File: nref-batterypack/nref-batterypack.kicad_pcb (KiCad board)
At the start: 2 copper layers, 75 x 18 mm, 6 parts

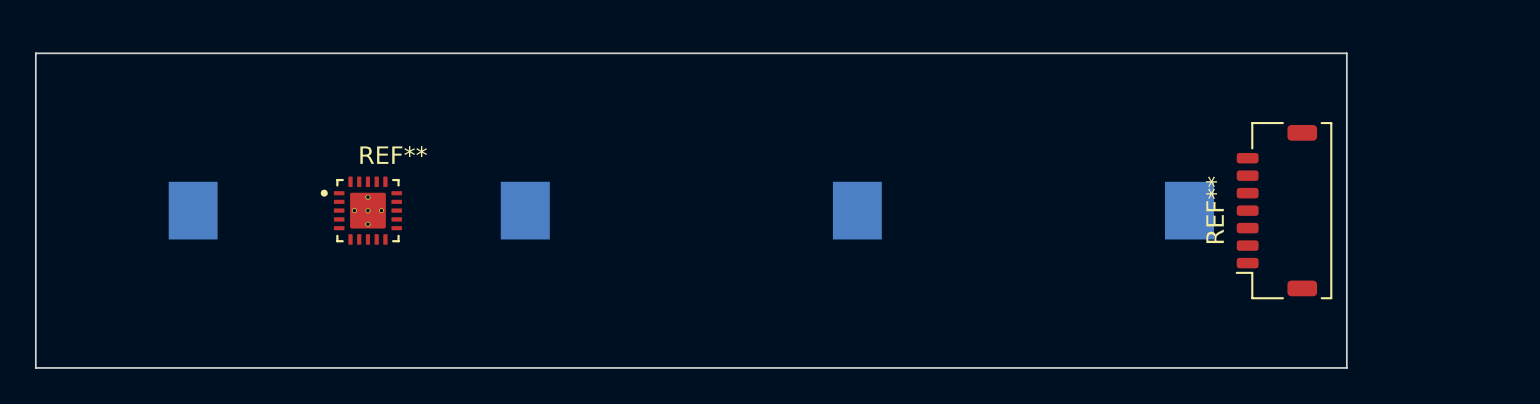
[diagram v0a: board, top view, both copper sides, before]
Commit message: add initial 4S battery pack with hs-switch
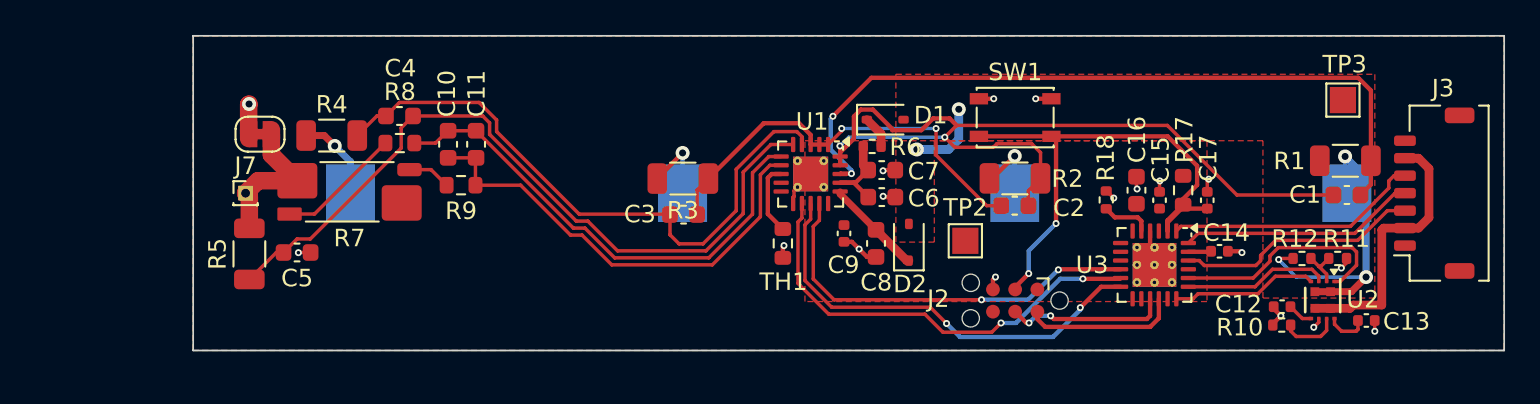
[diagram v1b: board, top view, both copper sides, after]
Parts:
- removed J** (x4): S713145R, footprints:S713145R
- removed REF**: JST_SHL_SM07B-SHLS-TF_1x07-1MP_P1.00mm_Horizontal, Connector_JST:JST_SHL_SM07B-SHLS-TF_1x07-1MP_P1.00mm_Horizontal
- removed REF**: IC_BQ76905RGRR, footprints:IC_BQ76905RGRR
- added C1: 220nF, Capacitor_SMD:C_0603_1608Metric, F.Cu at (166.0, 99.1)
- added C10: 100pF, Capacitor_SMD:C_0603_1608Metric, F.Cu at (114.6, 96.2)
- added C11: 100nF, Capacitor_SMD:C_0603_1608Metric, F.Cu at (116.2, 96.2)
- added C12: 2.2nF, Capacitor_SMD:C_0402_1005Metric, F.Cu at (162.3, 105.5)
- added C13: DNP, Capacitor_SMD:C_0402_1005Metric, F.Cu at (167.1, 106.3)
- added C14: 0.47uF, Capacitor_SMD:C_0402_1005Metric, F.Cu at (158.7, 102.3)
- added C15: 100nF, Capacitor_SMD:C_0402_1005Metric, F.Cu at (155.3, 99.4)
- added C16: 10uF, Capacitor_SMD:C_0603_1608Metric, F.Cu at (154.0, 98.8)
- added C17: 100nF, Capacitor_SMD:C_0402_1005Metric, F.Cu at (158.0, 99.4)
- added C2: 220nF, Capacitor_SMD:C_0603_1608Metric, F.Cu at (147.0, 99.7)
- added C3: 220nF, Capacitor_SMD:C_0603_1608Metric, F.Cu at (128.1, 100.2)
- added C4: 220nF, Capacitor_SMD:C_0603_1608Metric, F.Cu at (111.8, 94.6)
- added C5: 220nF, Capacitor_SMD:C_0603_1608Metric, F.Cu at (105.9, 102.4)
- added C6: 100pF/25V, Capacitor_SMD:C_0603_1608Metric, F.Cu at (139.4, 99.2)
- added C7: 1uF/25V, Capacitor_SMD:C_0603_1608Metric, F.Cu at (139.4, 97.7)
- added C8: 1uF/25V, Capacitor_SMD:C_0603_1608Metric, F.Cu at (139.1, 101.9)
- added C9: 1uF, Capacitor_SMD:C_0402_1005Metric, F.Cu at (137.2, 101.3)
- added D1: 40V, Diode_SMD:D_SOD-323, F.Cu at (139.6, 94.8)
- added D2: 40V, Diode_SMD:D_SOD-323, F.Cu at (140.9, 101.8)
- added J1: C3+, footprints:S713145R, B.Cu at (147.0, 99.0)
- added J2: DBG, Connector:Tag-Connect_TC2030-IDC-NL_2x03_P1.27mm_Vertical, F.Cu at (147.0, 105.1)
- added J3: PACK_CONN, Connector_JST:JST_SHL_SM07B-SHLS-TF_1x07-1MP_P1.00mm_Horizontal, F.Cu at (171.0, 99.0)
- added J4: C4+, footprints:S713145R, B.Cu at (166.0, 99.0)
- added J5: C2+, footprints:S713145R, B.Cu at (128.0, 99.0)
- added J6: C1+, footprints:S713145R, B.Cu at (109.0, 99.0)
- added J7: C1-, Connector_PinHeader_1.00mm:PinHeader_1x01_P1.00mm_Vertical, F.Cu at (103.0, 99.0)
- added NT1: P- to GND, Jumper:SolderJumper-2_P1.3mm_Bridged_RoundedPad1.0x1.5mm, F.Cu at (103.8, 95.6)
- added R1: 10R, Resistor_SMD:R_1206_3216Metric, F.Cu at (165.9, 97.1)
- added R10: 866R, Resistor_SMD:R_0402_1005Metric, F.Cu at (162.3, 106.5)
- added R11: 14.7k, Resistor_SMD:R_0402_1005Metric, F.Cu at (165.5, 102.7)
- added R12: 470k, Resistor_SMD:R_0402_1005Metric, F.Cu at (163.4, 102.7)
- added R17: 100R, Resistor_SMD:R_0603_1608Metric, F.Cu at (156.6, 98.8)
- added R18: 100k/0.1%/25ppm, Resistor_SMD:R_0402_1005Metric, F.Cu at (152.2, 99.4)
- added R2: 10R, Resistor_SMD:R_1206_3216Metric, F.Cu at (147.0, 98.2)
- added R3: 10R, Resistor_SMD:R_1206_3216Metric, F.Cu at (128.0, 98.2)
- added R4: 10R, Resistor_SMD:R_1206_3216Metric, F.Cu at (107.9, 95.7)
- added R5: 10R, Resistor_SMD:R_1206_3216Metric, F.Cu at (103.2, 102.5)
- added R6: 100R, Resistor_SMD:R_0402_1005Metric, F.Cu at (138.8, 96.3)
- added R7: 1u, Resistor_SMD:R_Shunt_Vishay_WSK2512_6332Metric_T1.19mm, F.Cu at (108.9, 98.9)
- added R8: 100R, Resistor_SMD:R_0603_1608Metric, F.Cu at (111.8, 96.1)
- added R9: 100R, Resistor_SMD:R_0603_1608Metric, F.Cu at (115.3, 98.5)
- added SW1: Reset, Button_Switch_SMD:SW_SPST_PTS810, F.Cu at (147.0, 94.7)
- added TH1: Thermistor, Resistor_SMD:R_0603_1608Metric, F.Cu at (133.7, 101.9)
- added TP2: 3V3, TestPoint:TestPoint_Pad_1.5x1.5mm, F.Cu at (144.2, 101.7)
- added TP3: Pack Voltage, TestPoint:TestPoint_Pad_1.5x1.5mm, F.Cu at (165.8, 93.7)
- added U1: BQ76905, Package_DFN_QFN:QFN-20-1EP_3.5x3.5mm_P0.5mm_EP2x2mm_ThermalVias, F.Cu at (135.3, 97.9)
- added U2: TPS259482, Automated:PowerWCSP12_YWP_TEX, F.Cu at (164.6, 105.1)
- added U3: MSPM0L130xRGE, Package_DFN_QFN:VQFN-24-1EP_4x4mm_P0.5mm_EP2.5x2.5mm_ThermalVias, F.Cu at (155.0, 103.1)
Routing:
- net Net-(U1-VC4A): track 0.00 -> 50.9 mm, vias 0 -> 2
- net Net-(U1-VC0): track 0.00 -> 43.1 mm
- net Net-(U1-VC5): track 0.00 -> 42.7 mm, vias 0 -> 2
- net Net-(U1-VC1): track 0.00 -> 35.3 mm
- net /~{RST}: track 0.00 -> 30.5 mm, vias 0 -> 2
- net Net-(U1-SRP): track 0.00 -> 28.1 mm
- net Net-(U1-SRN): track 0.00 -> 26.3 mm
- net /SCL_{DEV}: track 0.00 -> 25.6 mm, vias 0 -> 2
- net /SDA_{DEV}: track 0.00 -> 25.2 mm, vias 0 -> 2
- net Net-(U1-VC2): track 0.00 -> 24.4 mm, vias 0 -> 2
- net IN: track 0.00 -> 23.4 mm, vias 0 -> 5
- net /ALERT: track 0.00 -> 23.3 mm, vias 0 -> 2
- net GND: track 0.00 -> 20.3 mm, vias 0 -> 18
- net /V_{OUT}: track 0.00 -> 15.6 mm
- net /SCL_{HOST}: track 0.00 -> 14.6 mm
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- added copper zone on F.Cu, net +3V3
- added copper zone on F.Cu, net /PACK-
- added copper zone on B.Cu, net GND
- added copper zone on F.Cu, net IN
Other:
- board text removed: "consider S7091-42R (gold plated)"

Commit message: wip of the new version with another bms ic
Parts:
- removed C12: 2.2nF, Capacitor_SMD:C_0402_1005Metric
- removed C2, C3, C4, C5: 220nF, Capacitor_SMD:C_0603_1608Metric
- removed C8: 1uF/25V, Capacitor_SMD:C_0603_1608Metric
- removed J2: DBG, Connector:Tag-Connect_TC2030-IDC-NL_2x03_P1.27mm_Vertical
- removed TP2: 3V3, TestPoint:TestPoint_Pad_1.5x1.5mm
- removed U1: BQ76905, Package_DFN_QFN:QFN-20-1EP_3.5x3.5mm_P0.5mm_EP2x2mm_ThermalVias
- removed U2: TPS259482, Automated:PowerWCSP12_YWP_TEX
- removed U3: MSPM0L130xRGE, Package_DFN_QFN:VQFN-24-1EP_4x4mm_P0.5mm_EP2.5x2.5mm_ThermalVias
- added D3: 30V, Diode_SMD:D_SOD-323F, F.Cu at (157.8, 97.2)
- added D4: 30V, Diode_SMD:D_SOD-323F, F.Cu at (143.3, 97.5)
- added D5: 30V, Diode_SMD:D_SOD-323F, F.Cu at (123.7, 103.6)
- added D6: 30V, Diode_SMD:D_SOD-323F, F.Cu at (109.6, 105.0)
- added Q1: BC817, Package_TO_SOT_SMD:SOT-23, F.Cu at (157.7, 94.3)
- added Q10: 30V, Package_SON:Diodes_PowerDI3333-8, F.Cu at (130.9, 82.9)
- added Q2: BC817, Package_TO_SOT_SMD:SOT-23, F.Cu at (142.6, 94.7)
- added Q3: BC817, Package_TO_SOT_SMD:SOT-23, F.Cu at (123.7, 100.7)
- added Q4: BC817, Package_TO_SOT_SMD:SOT-23, F.Cu at (106.5, 102.7)
- added Q5: AO3401A, Package_TO_SOT_SMD:SOT-23, F.Cu at (135.9, 77.9)
- added Q6: AO3401A, Package_TO_SOT_SMD:SOT-23, F.Cu at (135.9, 82.5)
- added Q9: 30V, Package_SON:Diodes_PowerDI3333-8, F.Cu at (130.9, 78.0)
- added R13: 49.9R, Resistor_SMD:R_1206_3216Metric, F.Cu at (147.0, 95.2)
- added R14: 240R, Resistor_SMD:R_0603_1608Metric, F.Cu at (144.2, 100.0)
- added R15: 100R, Resistor_SMD:R_0603_1608Metric, F.Cu at (142.6, 100.0)
- added R16: 49.9R, Resistor_SMD:R_1206_3216Metric, F.Cu at (128.0, 100.1)
- added R19: 100R, Resistor_SMD:R_0603_1608Metric, F.Cu at (127.2, 103.6)
- added R20: 49.9R, Resistor_SMD:R_1206_3216Metric, F.Cu at (111.0, 102.1)
- added R21: 240R, Resistor_SMD:R_0603_1608Metric, F.Cu at (112.1, 104.0)
- added R22: 100R, Resistor_SMD:R_0603_1608Metric, F.Cu at (112.1, 105.6)
- added R23: 10M, Resistor_SMD:R_0603_1608Metric, F.Cu at (119.9, 63.6)
- added R24: 5.1k, Resistor_SMD:R_0603_1608Metric, F.Cu at (119.9, 66.1)
- added R25: 5.1k, Resistor_SMD:R_0603_1608Metric, F.Cu at (119.9, 68.6)
- added R26: 1k, Resistor_SMD:R_1206_3216Metric, F.Cu at (130.9, 73.8)
- added R27: 10k, Resistor_SMD:R_0603_1608Metric, F.Cu at (119.9, 71.1)
- added R28: 10k, Resistor_SMD:R_0603_1608Metric, F.Cu at (119.9, 73.6)
- added U4: BQ76922, Package_DFN_QFN:Texas_RSN_WQFN-32-1EP_4x4mm_P0.4mm_EP2.8x2.8mm, F.Cu at (136.8, 99.1)
- C1: value 220nF -> 470nF/25V
- C13: value DNP -> 220nF; footprint Capacitor_SMD:C_0402_1005Metric -> Capacitor_SMD:C_0603_1608Metric
- C14: value 0.47uF -> 220nF; footprint Capacitor_SMD:C_0402_1005Metric -> Capacitor_SMD:C_0603_1608Metric
- C15: value 100nF -> 220nF; footprint Capacitor_SMD:C_0402_1005Metric -> Capacitor_SMD:C_0603_1608Metric
- C16: value 10uF -> 220nF
- C9: value 1uF -> 2.2uF
- R1, R2, R5: value 10R -> 10M; footprint Resistor_SMD:R_1206_3216Metric -> Resistor_SMD:R_0603_1608Metric
- R10: value 866R -> 49.9R; footprint Resistor_SMD:R_0402_1005Metric -> Resistor_SMD:R_1206_3216Metric
- R11: value 14.7k -> 100R; footprint Resistor_SMD:R_0402_1005Metric -> Resistor_SMD:R_0603_1608Metric
- R12: value 470k -> 240R; footprint Resistor_SMD:R_0402_1005Metric -> Resistor_SMD:R_0603_1608Metric
- R18: value 100k/0.1%/25ppm -> 240R; footprint Resistor_SMD:R_0402_1005Metric -> Resistor_SMD:R_0603_1608Metric
- R3, R4: value 10R -> 5.1k; footprint Resistor_SMD:R_1206_3216Metric -> Resistor_SMD:R_0603_1608Metric
- moved C16 38.0 mm to (117.5, 109.6), turned to 180 degrees
- moved C1 30.7 mm to (135.5, 95.6)
- moved C17 28.5 mm to (172.4, 74.8)
- moved R17 28.5 mm to (171.0, 74.2)
- moved D2 25.8 mm to (150.1, 77.7)
- moved C9 25.8 mm to (146.4, 77.2)
- moved TH1 25.8 mm to (142.9, 77.8)
- moved R18 25.2 mm to (127.2, 102.0), turned to 180 degrees
- moved C15 24.4 mm to (133.2, 109.9), turned to 180 degrees
- moved SW1 19.2 mm to (158.1, 79.0)
- moved C14 15.4 mm to (145.3, 109.9)
- moved R10 12.9 mm to (162.0, 93.7), turned to 180 degrees
- moved R4 10.9 mm to (111.4, 85.4)
- moved R11 9.12 mm to (156.9, 99.7), turned to 90 degrees
- moved C6 8.85 mm to (131.7, 94.9), turned to -90 degrees
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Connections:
- net Net-(U1-SRN) renamed /SRN
- net Net-(U1-SRP) renamed /SRP
- C1 pad 1: Net-(U1-VC5) -> Net-(U4-CP1)
- C1 pad 2: Net-(U1-VC4A) -> Net-(U4-BAT)
- C13 pad 1: GND -> /BAT+
- C13 pad 2: Net-(U2-ITIMER) -> /VC4
- C14 pad 1: Net-(U3-V_{CORE}) -> /VC4
- C14 pad 2: GND -> /VC2
- C15 pad 1: GND -> /VC2
- C15 pad 2: +3V3 -> /VC1
- C16 pad 1: GND -> /VC1
- C16 pad 2: +3V3 -> /VC0
- C6 pad 1: Net-(U1-BAT) -> Net-(U4-BAT)
- C7 pad 1: Net-(U1-BAT) -> Net-(U4-BAT)
- C9 pad 1: +3V3 -> GND
- C9 pad 2: GND -> +1V8
- D1 pad 2: IN -> /BAT+
- J1 pad 1: Net-(J1-Pin_1) -> Net-(D3-A)
- J3 pad 2: /V_{OUT} -> /PACK+
- J3 pad 3: /IRQ -> /ALERT
- J3 pad 6: /V_{OUT} -> /PACK+
- J4 pad 1: IN -> /BAT+
- J5 pad 1: Net-(J5-Pin_1) -> Net-(D4-A)
- J6 pad 1: Net-(J6-Pin_1) -> Net-(D5-A)
- R1 pad 1: Net-(U1-VC5) -> Net-(D2-K)
- R1 pad 2: IN -> /BAT+
- R10 pad 1: GND -> /BAT+
- R11 pad 1: GND -> /VC4
- R11 pad 2: Net-(U2-OVLO) -> Net-(D3-A)
- R12 pad 1: Net-(U2-OVLO) -> /VC4
- R12 pad 2: IN -> Net-(D3-K)
- R17 pad 2: +3V3 -> +1V8
- R18 pad 1: GND -> /VC1
- R2 pad 1: Net-(U1-VC4A) -> Net-(D7-K)
- R2 pad 2: Net-(J1-Pin_1) -> /PACK+
- R3 pad 1: Net-(U1-VC2) -> /CHG
- R3 pad 2: Net-(J5-Pin_1) -> Net-(D2-K)
- R4 pad 1: Net-(U1-VC1) -> /DSG
- R4 pad 2: Net-(J6-Pin_1) -> Net-(D7-K)
- R5 pad 2: /BAT- -> Net-(Q5-S)
- R6 pad 1: Net-(U1-BAT) -> Net-(U4-BAT)
- TP3 pad 1: IN -> /BAT+
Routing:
- net Net-(U1-VC4A): track 50.9 -> 0.00 mm, vias 2 -> 0
- net Net-(Q5-G): track 43.1 -> 0.00 mm
- net Net-(U1-VC5): track 42.7 -> 0.00 mm, vias 2 -> 0
- net Net-(U1-VC1): track 35.3 -> 0.00 mm
- net /~{RST}: track 30.5 -> 0.00 mm, vias 2 -> 0
- net /SCL_{DEV}: track 25.6 -> 0.00 mm, vias 2 -> 0
- net /SDA_{DEV}: track 25.2 -> 0.00 mm, vias 2 -> 0
- net Net-(U1-VC2): track 24.4 -> 0.00 mm, vias 2 -> 0
- net /SRP: track 28.1 -> 3.83 mm
- net IN: track 23.4 -> 0.00 mm, vias 5 -> 0
- net /ALERT: track 23.3 -> 0.00 mm, vias 2 -> 0
- net /SRN: track 26.3 -> 3.18 mm
- net GND: track 20.3 -> 1.74 mm, vias 18 -> 1
- net /V_{OUT}: track 15.6 -> 0.00 mm
- net /SCL_{HOST}: track 14.6 -> 0.00 mm
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- removed copper zone on F.Cu, net +3V3
- removed copper zone on F.Cu, net /PACK-
- removed copper zone on B.Cu, net GND
- removed copper zone on F.Cu, net IN
